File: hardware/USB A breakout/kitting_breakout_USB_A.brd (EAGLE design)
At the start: 17.7 x 21.3 mm, 5 parts, among them J3 USB_A

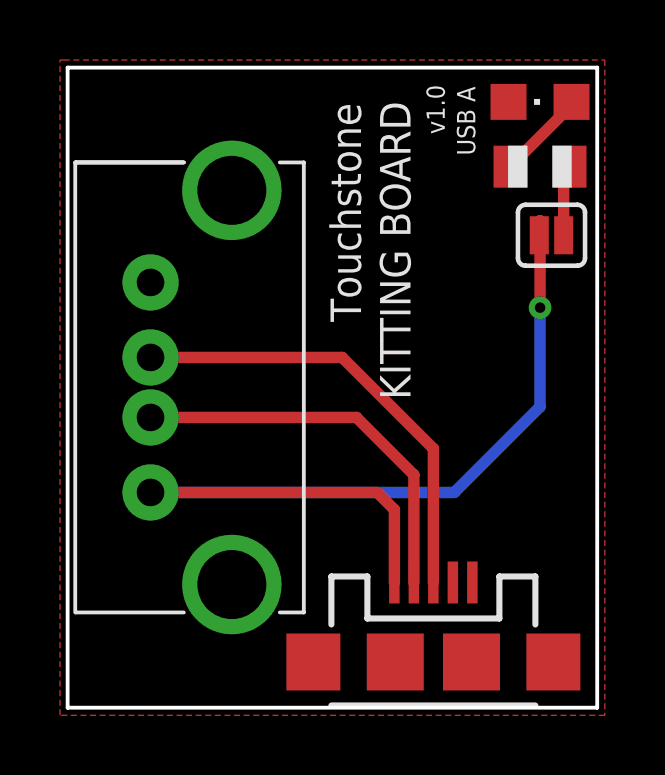
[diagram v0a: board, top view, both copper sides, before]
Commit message: Added mounting hole on USB A breakout
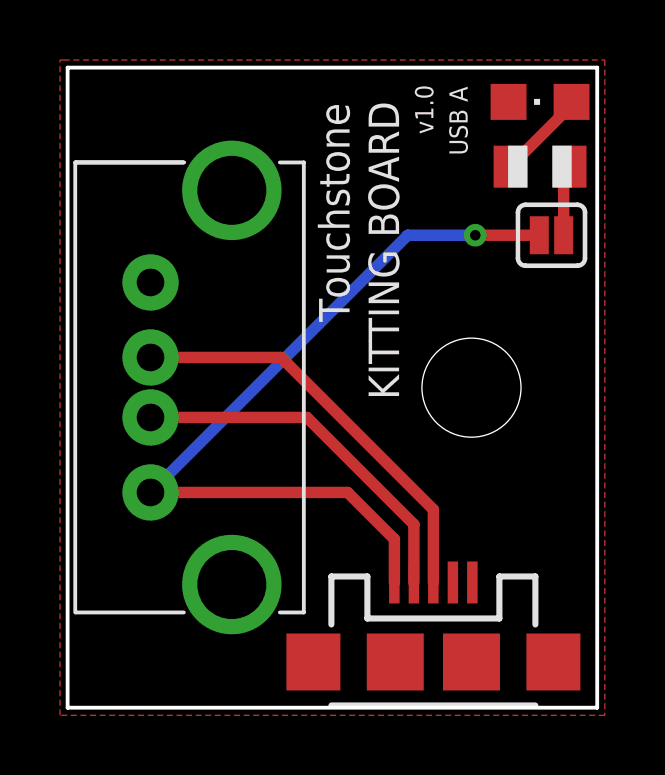
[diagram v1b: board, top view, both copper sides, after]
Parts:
- added H1: STAND-OFF, SparkFun-Hardware:STAND-OFF
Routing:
- net VCC1: track 31.6 -> 26.7 mm
- net D+: track 15.1 -> 14.0 mm
- net D-: track 13.2 -> 12.2 mm
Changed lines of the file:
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@@
 <board>
 <plain>
-<text x="9.779" y="16.51" size="1.016" layer="21" font="vector" rot="SR90" align="bottom-center">Touchstone</text>
-<text x="10.414" y="15.24" size="1.016" layer="21" font="vector" ratio="12" rot="R270" align="bottom-center">KITTING BOARD</text>
-<text x="12.573" y="19.939" size="0.6096" layer="21" font="vector" ratio="5" rot="R90" align="bottom-center">v1.0</text>
-<text x="17.018" y="10.668" size="0.8128" layer="22" font="vector" rot="SMR270" align="bottom-center">Designed by Akram Ali</text>
+<text x="9.398" y="16.51" size="1.016" layer="21" font="vector" rot="SR90" align="bottom-center">Touchstone</text>
+<text x="10.033" y="15.24" size="1.016" layer="21" font="vector" ratio="12" rot="R270" align="bottom-center">KITTING BOARD</text>
+<text x="12.192" y="19.939" size="0.6096" layer="21" font="vector" ratio="5" rot="R90" align="bottom-center">v1.0</text>
+<text x="17.145" y="10.668" size="0.8128" layer="22" font="vector" rot="SMR270" align="bottom-center">Designed by Akram Ali</text>
 <wire x1="0" y1="0" x2="0" y2="21.336" width="0.127" layer="20"/>
 <wire x1="0" y1="21.336" x2="17.653" y2="21.336" width="0.127" layer="20"/>
 <wire x1="17.653" y1="21.336" x2="17.653" y2="0" width="0.127" layer="20"/>
 <wire x1="17.653" y1="0" x2="0" y2="0" width="0.127" layer="20"/>
-<text x="13.589" y="19.558" size="0.6096" layer="21" font="vector" rot="R90" align="bottom-center">USB A</text>
+<text x="13.335" y="19.558" size="0.6096" layer="21" font="vector" rot="R90" align="bottom-center">USB A</text>
 </plain>
 <attributes>
@@
 </element>
 <element name="J3" library="USB_A_female_VRT" package="USB-A-H-FEMALE-VRT-PTH" value="USB_A" x="7.874" y="3.175" smashed="yes" rot="R90"/>
+<element name="H1" library="SparkFun-Hardware" package="STAND-OFF" value="STAND-OFF" x="13.462" y="10.668" smashed="yes"/>
 </elements>
 <signals>
@@
 <signal name="D+">
 <contactref element="J2" pad="D+"/>
-<wire x1="12.192" y1="8.636" x2="12.192" y2="4.174" width="0.381" layer="1"/>
 <contactref element="J3" pad="D+"/>
-<wire x1="2.764" y1="11.675" x2="9.153" y2="11.675" width="0.381" layer="1"/>
-<wire x1="9.153" y1="11.675" x2="12.192" y2="8.636" width="0.381" layer="1"/>
+<wire x1="12.192" y1="6.604" x2="12.192" y2="4.174" width="0.381" layer="1"/>
+<wire x1="2.764" y1="11.675" x2="7.121" y2="11.675" width="0.381" layer="1"/>
+<wire x1="7.121" y1="11.675" x2="12.192" y2="6.604" width="0.381" layer="1"/>
 </signal>
 <signal name="N$6">
@@
 <contactref element="JP7" pad="2"/>
 <contactref element="J2" pad="VBUS"/>
-<wire x1="10.892" y1="6.604" x2="10.892" y2="4.174" width="0.381" layer="1"/>
-<via x="15.748" y="13.335" extent="1-16" drill="0.35"/>
-<wire x1="15.748" y1="13.335" x2="15.748" y2="16.2306" width="0.381" layer="1"/>
-<wire x1="15.748" y1="16.2306" x2="15.7226" y2="15.748" width="0.381" layer="1"/>
 <contactref element="J3" pad="VBUS"/>
-<wire x1="2.764" y1="7.175" x2="10.321" y2="7.175" width="0.381" layer="1"/>
-<wire x1="10.321" y1="7.175" x2="10.892" y2="6.604" width="0.381" layer="1"/>
-<wire x1="15.748" y1="10.033" x2="15.748" y2="13.335" width="0.381" layer="16"/>
-<wire x1="2.764" y1="7.175" x2="12.89" y2="7.175" width="0.381" layer="16"/>
-<wire x1="12.89" y1="7.175" x2="15.748" y2="10.033" width="0.381" layer="16"/>
+<wire x1="10.892" y1="5.618" x2="10.892" y2="4.174" width="0.381" layer="1"/>
+<wire x1="2.764" y1="7.175" x2="9.335" y2="7.175" width="0.381" layer="1"/>
+<wire x1="9.335" y1="7.175" x2="10.892" y2="5.618" width="0.381" layer="1"/>
+<wire x1="15.7226" y1="15.748" x2="13.589" y2="15.748" width="0.381" layer="1"/>
+<via x="13.589" y="15.748" extent="1-16" drill="0.35"/>
+<wire x1="13.589" y1="15.748" x2="11.337" y2="15.748" width="0.381" layer="16"/>
+<wire x1="11.337" y1="15.748" x2="2.764" y2="7.175" width="0.381" layer="16"/>
 </signal>
 <signal name="D-">
 <contactref element="J3" pad="D-"/>
 <contactref element="J2" pad="D-"/>
-<wire x1="11.542" y1="7.762" x2="11.542" y2="4.174" width="0.381" layer="1"/>
-<wire x1="2.764" y1="9.675" x2="9.629" y2="9.675" width="0.381" layer="1"/>
-<wire x1="9.629" y1="9.675" x2="11.542" y2="7.762" width="0.381" layer="1"/>
+<wire x1="7.978" y1="9.675" x2="2.764" y2="9.675" width="0.381" layer="1"/>
+<wire x1="11.542" y1="4.174" x2="11.542" y2="6.111" width="0.381" layer="1"/>
+<wire x1="11.542" y1="6.111" x2="7.978" y2="9.675" width="0.381" layer="1"/>
 </signal>
 </signals>
